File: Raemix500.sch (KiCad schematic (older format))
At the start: 0 parts

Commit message: Add Denise & Video
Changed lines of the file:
@@
 $Descr A4 11693 8268
 encoding utf-8
-Sheet 1 3
+Sheet 1 4
 Title "Rämixx500"
 Date "2019-04-14"
@@
 F1 "ram.sch" 50
 $EndSheet
+$Sheet
+S 1345 4210 1305 865
+U 5CBA5669
+F0 "Denise & Video Stuff" 50
+F1 "video.sch" 50
+$EndSheet
 $EndSCHEMATC

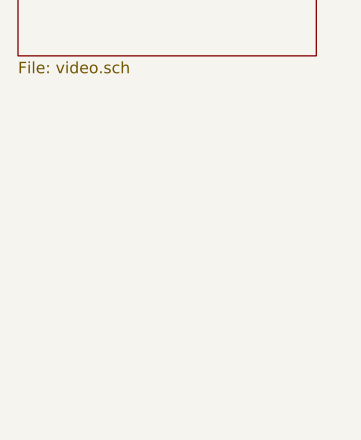
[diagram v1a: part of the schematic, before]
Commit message: Add Paula and Joystick Ports, audio filters still missing
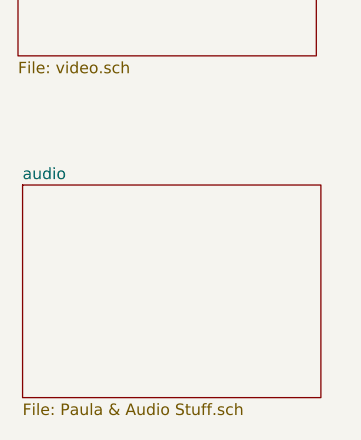
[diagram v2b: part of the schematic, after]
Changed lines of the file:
@@
 $Descr A4 11693 8268
 encoding utf-8
-Sheet 1 4
+Sheet 1 5
 Title "Rämixx500"
-Date "2019-04-14"
+Date "2019-04-15"
 Rev "1git"
 Comp "SukkoPera"
@@
 F1 "video.sch" 50
 $EndSheet
+$Sheet
+S 1365 5640 1305 930
+U 5D2DC3A1
+F0 "audio" 50
+F1 "Paula & Audio Stuff.sch" 50
+$EndSheet
 $EndSCHEMATC

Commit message: Rename audio schematics
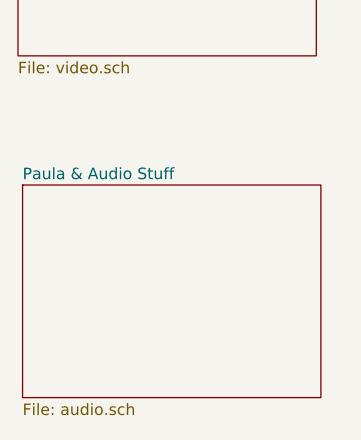
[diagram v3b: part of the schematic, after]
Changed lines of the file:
@@
 S 1365 5640 1305 930
 U 5D2DC3A1
-F0 "audio" 50
-F1 "Paula & Audio Stuff.sch" 50
+F0 "Paula & Audio Stuff" 50
+F1 "audio.sch" 50
 $EndSheet
 $EndSCHEMATC
